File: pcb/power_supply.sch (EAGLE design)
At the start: 3 parts, among them IC1 L78S05CV

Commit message: pcb - connectors, raspberry
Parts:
- added U1: RASPBERRY_PI_3_MODEL_B+, RASPBERRY_PI_3_MODEL_B_:RASPBERRY_PI_3_MODEL_B+
- added X1, X2, X3, X4: MKKDS02, con-phoenix-508:MKKDS02
- added X5: MKDSN1,5/2-5,08, con-phoenix-508:MKDSN1,5/2-5,08
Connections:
- removed net 5V: C2.1, IC1.OUT
- new net 5V_2A: C2.1, IC1.OUT, U1.5V0
- net 12V: now also X5-1.KL
- net GND: now also U1.GND, X1-1.KL, X1-2.KL, X2-1.KL, X2-2.KL, X3-1.KL, X3-2.KL, X4-1.KL, X4-2.KL, X5-2.KL
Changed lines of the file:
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@@
 <part name="C2" library="rcl" library_urn="urn:adsk.eagle:library:334" deviceset="C-EU" device="C0805" package3d_urn="urn:adsk.eagle:package:23617/2" value="0.1uF"/>
 <part name="C1" library="rcl" library_urn="urn:adsk.eagle:library:334" deviceset="C-EU" device="C0805" package3d_urn="urn:adsk.eagle:package:23617/2" value="0.33uF"/>
+<part name="U1" library="RASPBERRY_PI_3_MODEL_B_" deviceset="RASPBERRY_PI_3_MODEL_B+" device=""/>
+<part name="SUPPLY3" library="supply2" library_urn="urn:adsk.eagle:library:372" deviceset="GND" device=""/>
+<part name="X1" library="con-phoenix-508" library_urn="urn:adsk.eagle:library:176" deviceset="MKKDS02" device="" package3d_urn="urn:adsk.eagle:package:9589/1"/>
+<part name="X2" library="con-phoenix-508" library_urn="urn:adsk.eagle:library:176" deviceset="MKKDS02" device="" package3d_urn="urn:adsk.eagle:package:9589/1"/>
+<part name="X3" library="con-phoenix-508" library_urn="urn:adsk.eagle:library:176" deviceset="MKKDS02" device="" package3d_urn="urn:adsk.eagle:package:9589/1"/>
+<part name="X4" library="con-phoenix-508" library_urn="urn:adsk.eagle:library:176" deviceset="MKKDS02" device="" package3d_urn="urn:adsk.eagle:package:9589/1"/>
+<part name="X5" library="con-phoenix-508" library_urn="urn:adsk.eagle:library:176" deviceset="MKDSN1,5/2-5,08" device="" package3d_urn="urn:adsk.eagle:package:9630/1"/>
+<part name="SUPPLY2" library="supply2" library_urn="urn:adsk.eagle:library:372" deviceset="GND" device=""/>
+<part name="SUPPLY4" library="supply2" library_urn="urn:adsk.eagle:library:372" deviceset="GND" device=""/>
 </parts>
 <sheets>
@@
 <attribute name="VALUE" x="-6.096" y="71.501" size="1.778" layer="96"/>
 </instance>
+<instance part="U1" gate="G$1" x="2.54" y="10.16" smashed="yes">
+<attribute name="NAME" x="-20.32" y="38.1" size="1.27" layer="95"/>
+<attribute name="VALUE" x="-20.32" y="-27.305" size="1.27" layer="96"/>
+</instance>
+<instance part="SUPPLY3" gate="GND" x="30.48" y="-25.4" smashed="yes">
+<attribute name="VALUE" x="28.575" y="-28.575" size="1.778" layer="96"/>
+</instance>
+<instance part="X1" gate="-1" x="86.36" y="-43.18" smashed="yes">
+<attribute name="NAME" x="89.408" y="-44.069" size="1.778" layer="95"/>
+</instance>
+<instance part="X1" gate="-2" x="86.36" y="-48.26" smashed="yes">
+<attribute name="NAME" x="89.408" y="-49.149" size="1.778" layer="95"/>
+</instance>
+<instance part="X1" gate="-3" x="86.36" y="-53.34" smashed="yes">
+<attribute name="NAME" x="89.408" y="-54.229" size="1.778" layer="95"/>
+</instance>
+<instance part="X1" gate="-4" x="86.36" y="-58.42" smashed="yes">
+<attribute name="NAME" x="89.408" y="-59.309" size="1.778" layer="95"/>
+<attribute name="VALUE" x="83.82" y="-62.103" size="1.778" layer="96"/>
+</instance>
+<instance part="X2" gate="-1" x="86.36" y="-66.04" smashed="yes">
+<attribute name="NAME" x="89.408" y="-66.929" size="1.778" layer="95"/>
+</instance>
+<instance part="X2" gate="-2" x="86.36" y="-71.12" smashed="yes">
+<attribute name="NAME" x="89.408" y="-72.009" size="1.778" layer="95"/>
+</instance>
+<instance part="X2" gate="-3" x="86.36" y="-76.2" smashed="yes">
+<attribute name="NAME" x="89.408" y="-77.089" size="1.778" layer="95"/>
+</instance>
+<instance part="X2" gate="-4" x="86.36" y="-81.28" smashed="yes">
+<attribute name="NAME" x="89.408" y="-82.169" size="1.778" layer="95"/>
+<attribute name="VALUE" x="83.82" y="-84.963" size="1.778" layer="96"/>
+</instance>
+<instance part="X3" gate="-1" x="86.36" y="-88.9" smashed="yes">
+<attribute name="NAME" x="89.408" y="-89.789" size="1.778" layer="95"/>
+</instance>
+<instance part="X3" gate="-2" x="86.36" y="-93.98" smashed="yes">
+<attribute name="NAME" x="89.408" y="-94.869" size="1.778" layer="95"/>
+</instance>
+<instance part="X3" gate="-3" x="86.36" y="-99.06" smashed="yes">
+<attribute name="NAME" x="89.408" y="-99.949" size="1.778" layer="95"/>
+</instance>
+<instance part="X3" gate="-4" x="86.36" y="-104.14" smashed="yes">
+<attribute name="NAME" x="89.408" y="-105.029" size="1.778" layer="95"/>
+<attribute name="VALUE" x="83.82" y="-107.823" size="1.778" layer="96"/>
+</instance>
+<instance part="X4" gate="-1" x="86.36" y="-111.76" smashed="yes">
+<attribute name="NAME" x="89.408" y="-112.649" size="1.778" layer="95"/>
+</instance>
+<instance part="X4" gate="-2" x="86.36" y="-116.84" smashed="yes">
+<attribute name="NAME" x="89.408" y="-117.729" size="1.778" layer="95"/>
+</instance>
+<instance part="X4" gate="-3" x="86.36" y="-121.92" smashed="yes">
+<attribute name="NAME" x="89.408" y="-122.809" size="1.778" layer="95"/>
+</instance>
+<instance part="X4" gate="-4" x="86.36" y="-127" smashed="yes">
+<attribute name="NAME" x="89.408" y="-127.889" size="1.778" layer="95"/>
+<attribute name="VALUE" x="83.82" y="-130.683" size="1.778" layer="96"/>
+</instance>
+<instance part="X5" gate="-1" x="-68.58" y="81.28" smashed="yes">
+<attribute name="NAME" x="-65.532" y="80.391" size="1.778" layer="95"/>
+<attribute name="VALUE" x="-71.12" y="77.597" size="1.778" layer="96"/>
+</instance>
+<instance part="X5" gate="-2" x="-68.58" y="76.2" smashed="yes">
+<attribute name="NAME" x="-65.532" y="75.311" size="1.778" layer="95"/>
+<attribute name="VALUE" x="-71.12" y="72.517" size="1.778" layer="96"/>
+</instance>
+<instance part="SUPPLY2" gate="GND" x="-81.28" y="73.66" smashed="yes">
+<attribute name="VALUE" x="-83.185" y="70.485" size="1.778" layer="96"/>
+</instance>
+<instance part="SUPPLY4" gate="GND" x="76.2" y="-134.62" smashed="yes">
+<attribute name="VALUE" x="74.295" y="-137.795" size="1.778" layer="96"/>
+</instance>
 </instances>
 <busses>
@@
 <junction x="-10.16" y="81.28"/>
 </segment>
+<segment>
+<pinref part="X5" gate="-1" pin="KL"/>
+<wire x1="-71.12" y1="81.28" x2="-81.28" y2="81.28" width="0.1524" layer="91"/>
+<label x="-81.28" y="81.28" size="1.778" layer="95"/>
+</segment>
 </net>
-<net name="5V" class="0">
+<net name="5V_2A" class="0">
 <segment>
 <pinref part="IC1" gate="G$1" pin="OUT"/>
@@
 <wire x1="33.02" y1="76.2" x2="33.02" y2="81.28" width="0.1524" layer="91"/>
 <junction x="33.02" y="81.28"/>
+</segment>
+<segment>
+<pinref part="U1" gate="G$1" pin="5V0"/>
+<wire x1="27.94" y1="33.02" x2="30.48" y2="33.02" width="0.1524" layer="91"/>
+<label x="30.48" y="33.02" size="1.778" layer="95"/>
 </segment>
 </net>
@@
 <wire x1="10.16" y1="73.66" x2="10.16" y2="68.58" width="0.1524" layer="91"/>
 </segment>
+<segment>
+<pinref part="U1" gate="G$1" pin="GND"/>
+<pinref part="SUPPLY3" gate="GND" pin="GND"/>
+<wire x1="27.94" y1="-22.86" x2="30.48" y2="-22.86" width="0.1524" layer="91"/>
+</segment>
+<segment>
+<pinref part="X5" gate="-2" pin="KL"/>
+<pinref part="SUPPLY2" gate="GND" pin="GND"/>
+<wire x1="-71.12" y1="76.2" x2="-81.28" y2="76.2" width="0.1524" layer="91"/>
+</segment>
+<segment>
+<pinref part="X1" gate="-1" pin="KL"/>
+<wire x1="83.82" y1="-43.18" x2="76.2" y2="-43.18" width="0.1524" layer="91"/>
+<pinref part="SUPPLY4" gate="GND" pin="GND"/>
+<wire x1="76.2" y1="-43.18" x2="76.2" y2="-48.26" width="0.1524" layer="91"/>
+<pinref part="X4" gate="-2" pin="KL"/>
+<wire x1="76.2" y1="-48.26" x2="76.2" y2="-66.04" width="0.1524" layer="91"/>
+<wire x1="76.2" y1="-66.04" x2="76.2" y2="-71.12" width="0.1524" layer="91"/>
+<wire x1="76.2" y1="-71.12" x2="76.2" y2="-88.9" width="0.1524" layer="91"/>
+<wire x1="76.2" y1="-88.9" x2="76.2" y2="-93.98" width="0.1524" layer="91"/>
+<wire x1="76.2" y1="-93.98" x2="76.2" y2="-111.76" width="0.1524" layer="91"/>
+<wire x1="76.2" y1="-111.76" x2="76.2" y2="-116.84" width="0.1524" layer="91"/>
+<wire x1="76.2" y1="-116.84" x2="76.2" y2="-132.08" width="0.1524" layer="91"/>
+<wire x1="83.82" y1="-116.84" x2="76.2" y2="-116.84" width="0.1524" layer="91"/>
+<junction x="76.2" y="-116.84"/>
+<pinref part="X4" gate="-1" pin="KL"/>
+<wire x1="83.82" y1="-111.76" x2="76.2" y2="-111.76" width="0.1524" layer="91"/>
+<junction x="76.2" y="-111.76"/>
+<pinref part="X3" gate="-2" pin="KL"/>
+<wire x1="83.82" y1="-93.98" x2="76.2" y2="-93.98" width="0.1524" layer="91"/>
+<junction x="76.2" y="-93.98"/>
+<pinref part="X3" gate="-1" pin="KL"/>
+<wire x1="83.82" y1="-88.9" x2="76.2" y2="-88.9" width="0.1524" layer="91"/>
+<junction x="76.2" y="-88.9"/>
+<pinref part="X2" gate="-2" pin="KL"/>
+<wire x1="83.82" y1="-71.12" x2="76.2" y2="-71.12" width="0.1524" layer="91"/>
+<junction x="76.2" y="-71.12"/>
+<pinref part="X2" gate="-1" pin="KL"/>
+<wire x1="83.82" y1="-66.04" x2="76.2" y2="-66.04" width="0.1524" layer="91"/>
+<junction x="76.2" y="-66.04"/>
+<pinref part="X1" gate="-2" pin="KL"/>
+<wire x1="83.82" y1="-48.26" x2="76.2" y2="-48.26" width="0.1524" layer="91"/>
+<junction x="76.2" y="-48.26"/>
+</segment>
 </net>

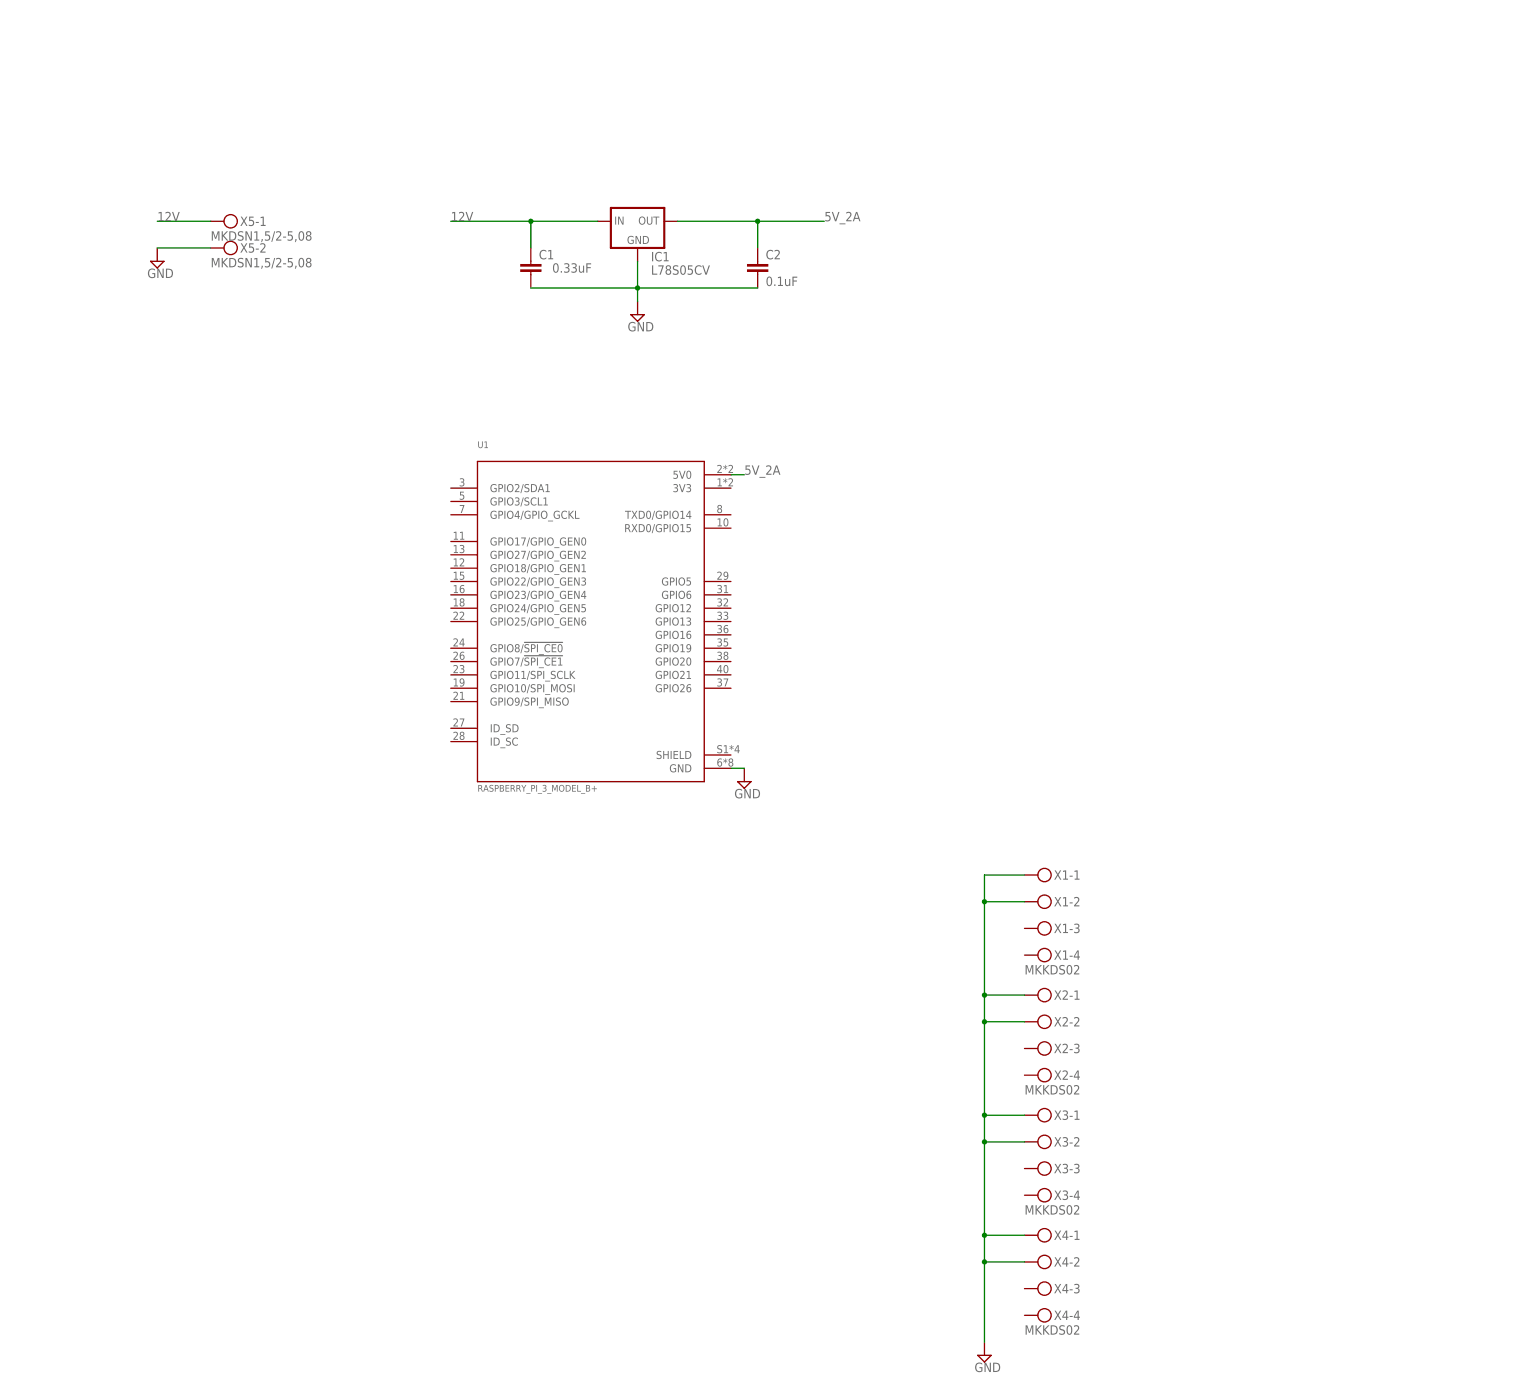
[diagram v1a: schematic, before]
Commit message: pcb - voltage regulators
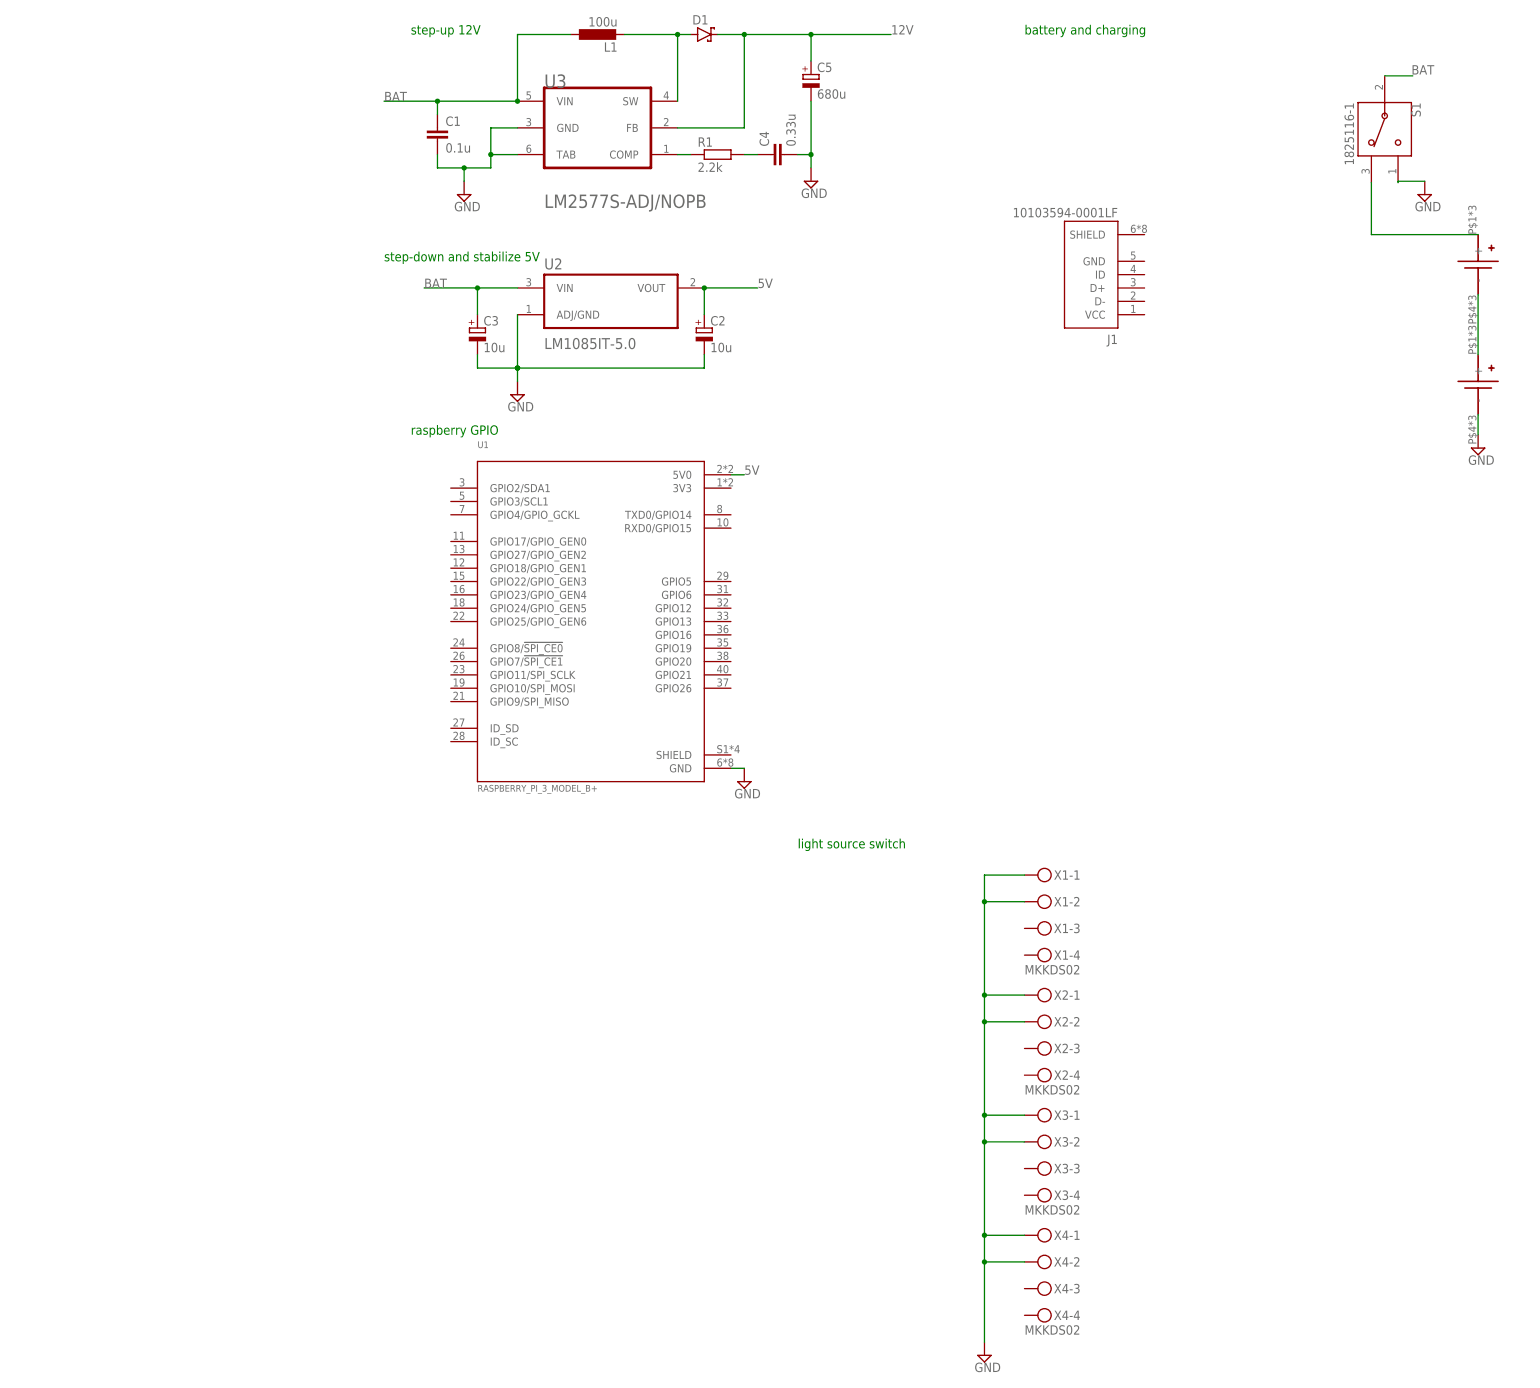
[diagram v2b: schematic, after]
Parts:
- removed IC1: L78S05CV, L78S05CV:L78S05CV
- removed X5: MKDSN1,5/2-5,08, con-phoenix-508:MKDSN1,5/2-5,08
- added C3: 10u, rcl:CPOL-EUSMCB
- added C4: 0.33u, rcl:C-EUC0805
- added C5: 680u, rcl:CPOL-EUSMCB
- added D1: (no value), diode:SCHOTTKY-DIODEDO35-7
- added J1: 10103594-0001LF, 10103594-0001LF:10103594-0001LF
- added L1: 100u, rcl:L-EU0207/5V
- added R1: 2.2k, rcl:R-EU_R0805
- added S1: 1825116-1, 1825116-1:1825116-1
- added U$1, U$2: KEYESTONE_54A_3D, battery-holders:KEYESTONE_54A_3D
- added U2: LM1085IT-5.0, LM1085IT-5.0:LM1085IT-5.0
- added U3: TI_NATIONAL_SEMICONDUCTOR_LM2577S-ADJ-NOPBTI_NATIONAL_SEMIC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, LM2577S-ADJ_NOPB:TI_NATIONAL_SEMICONDUCTOR_LM2577S-ADJ-NOPBTI_NATIONAL_SEMICONDUCTOR_LM2577S-ADJ-NOPB_0_2
- C1: value 0.33uF -> 0.1u
- C2: value 0.1uF -> 10u; device rcl:C-EUC0805 -> rcl:CPOL-EUSMCB
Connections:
- removed net 5V_2A: C2.1, IC1.OUT, U1.5V0
- new net 5V: C2.+, U1.5V0, U2.VOUT
- new net BAT: C1.1, C3.+, L1.1, S1.2, U2.VIN, U3.VIN
- new net N$1: U$1.-, U$2.+
- new net N$3: S1.3, U$1.+
- new net N$4: R1.1, U3.COMP
- new net N$5: D1.A, L1.2, U3.SW
- new net N$7: C4.1, R1.2
- net 12V: now also C5.+, D1.C, U3.FB; no longer C1.1, IC1.IN, X5-1.KL
- net GND: now also C2.-, C3.-, C4.2, C5.-, S1.1, U$2.-, U2.ADJ/GND, U3.GND, U3.TAB; no longer C2.2, IC1.GND, X5-2.KL
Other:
- note added: "battery and charging"
- note added: "light source switch"
- note added: "raspberry GPIO"
- note added: "step-down and stabilize 5V"
- note added: "step-up 12V"
- moved on the sheet: C1
